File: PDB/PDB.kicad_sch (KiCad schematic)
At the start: 42 parts, among them Q1 S8050, Sw1 D-SWITCH_MR5-111-C5N-BB

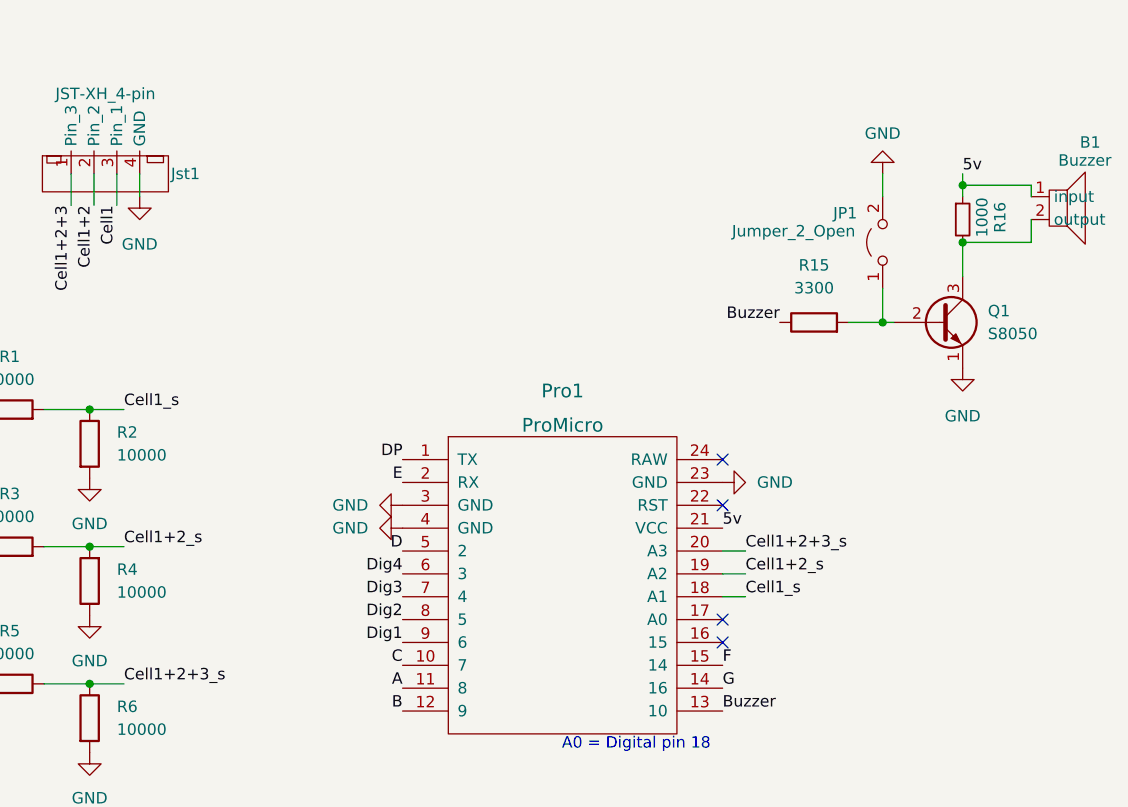
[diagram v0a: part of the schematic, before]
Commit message: Completed board layout
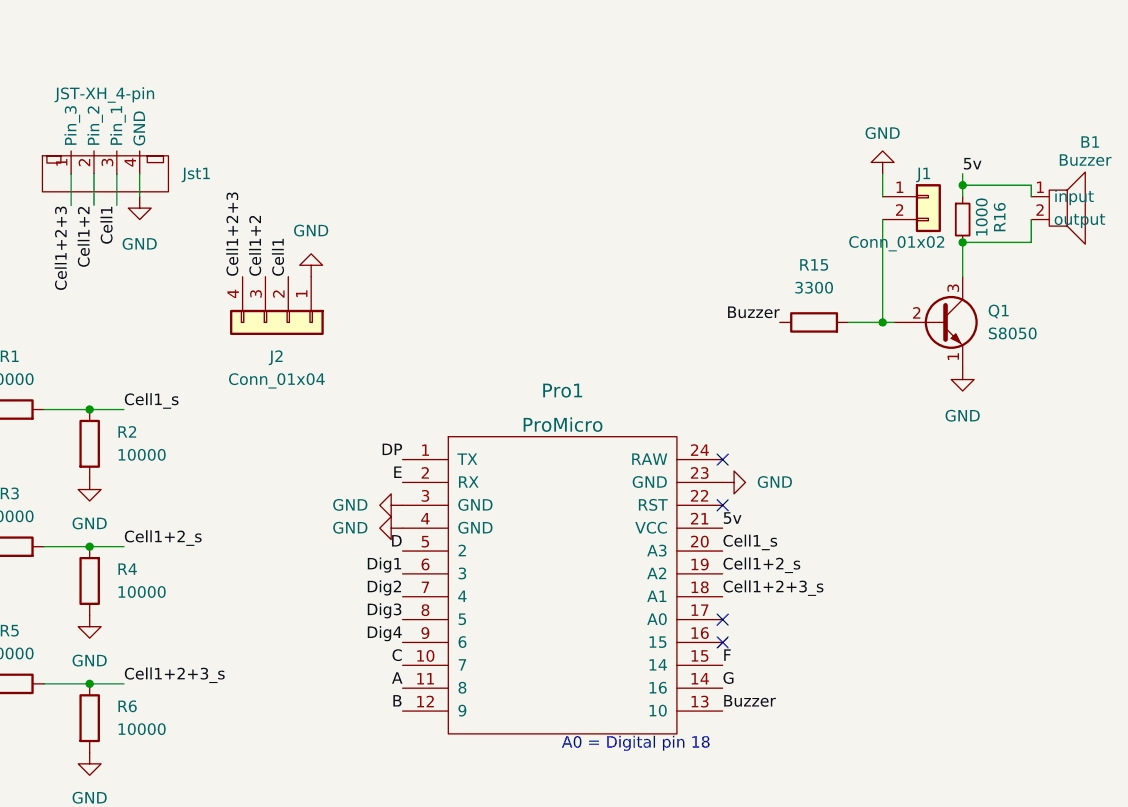
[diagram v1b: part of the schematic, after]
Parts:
- removed JP1: Jumper_2_Open, Connector_PinHeader_2.54mm:PinHeader_1x02_P2.54mm_Vertical, symbol Jumper:Jumper_2_Open
- added J1: Conn_01x02, Connector_PinHeader_2.54mm:PinHeader_1x02_P2.54mm_Vertical, symbol Connector_Generic:Conn_01x02
- added J2: Conn_01x04, Connector_PinHeader_2.54mm:PinHeader_1x04_P2.54mm_Vertical, symbol Connector_Generic:Conn_01x04
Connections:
- net Cell1: now also J2.2 (Pin_2)
- net Cell1+2: now also J2.3 (Pin_3)
- net Cell1+2+3: now also J2.4 (Pin_4)
- net Cell1+2+3_s: now also Pro1.18 (A1); no longer Pro1.20 (A3)
- net Cell1_s: now also Pro1.20 (A3); no longer Pro1.18 (A1)
- net Dig1: now also Pro1.6 (3); no longer Pro1.9 (6)
- net Dig2: now also Pro1.7 (4); no longer Pro1.8 (5)
- net Dig3: now also Pro1.8 (5); no longer Pro1.7 (4)
- net Dig4: now also Pro1.9 (6); no longer Pro1.6 (3)
- net GND: now also J1.1 (Pin_1), J2.1 (Pin_1)
- net at Q1.2 (B), R15.2: now also J1.2 (Pin_2)
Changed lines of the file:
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@@
-    (stroke (width 0) (type default) (color 0 0 0 0))
-  )
-  (wire (pts (xy 109.22 177.8) (xy 111.76 177.8))
     (stroke (width 0) (type default) (color 0 0 0 0))
   )
@@
     (stroke (width 0) (type default) (color 0 0 0 0))
   )
-  (wire (pts (xy 109.22 172.72) (xy 111.76 172.72))
-    (stroke (width 0) (type default) (color 0 0 0 0))
-  )
   (wire (pts (xy 36.83 130.81) (xy 36.83 134.31))
     (stroke (width 0) (type default) (color 0 0 0 0))
   )
-  (wire (pts (xy 127 143.51) (xy 127 147.32))
-    (stroke (width 0) (type default) (color 0 0 0 0))
-  )
-  (wire (pts (xy 109.22 175.26) (xy 111.76 175.26))
+  (wire (pts (xy 127 135.89) (xy 127 147.32))
     (stroke (width 0) (type default) (color 0 0 0 0))
   )
@@
     (effects (font (size 1.27 1.27)) (justify left bottom))
   )
-  (label "Cell1+2+3_s" (at 111.76 172.72 0)
+  (label "Cell1+2+3_s" (at 109.22 177.8 0)
     (effects (font (size 1.27 1.27)) (justify left bottom))
   )
@@
     (effects (font (size 1.27 1.27)) (justify right bottom))
   )
-  (label "Dig2" (at 73.66 180.34 180)
-    (effects (font (size 1.27 1.27)) (justify right bottom))
-  )
-  (label "Dig4" (at 73.66 175.26 180)
-    (effects (font (size 1.27 1.27)) (justify right bottom))
+  (label "Dig2" (at 73.66 177.8 180)
+    (effects (font (size 1.27 1.27)) (justify right bottom))
+  )
+  (label "Dig4" (at 73.66 182.88 180)
+    (effects (font (size 1.27 1.27)) (justify right bottom))
+  )
+  (label "Cell1+2+3" (at 55.88 142.24 90)
+    (effects (font (size 1.27 1.27)) (justify left bottom))
   )
   (label "12v" (at 53.41 55.45 0)
@@
     (effects (font (size 1.27 1.27)) (justify left bottom))
   )
+  (label "Cell1" (at 60.96 142.24 90)
+    (effects (font (size 1.27 1.27)) (justify left bottom))
+  )
   (label "Cell1+2+3" (at 36.83 134.31 270)
     (effects (font (size 1.27 1.27)) (justify right bottom))
@@
     (effects (font (size 1.27 1.27)) (justify left bottom))
   )
-  (label "Cell1_s" (at 111.76 177.8 0)
+  (label "Cell1_s" (at 109.22 172.72 0)
+    (effects (font (size 1.27 1.27)) (justify left bottom))
+  )
+  (label "Cell1+2" (at 58.42 142.24 90)
     (effects (font (size 1.27 1.27)) (justify left bottom))
   )
@@
     (effects (font (size 1.27 1.27)) (justify right bottom))
   )
-  (label "Dig3" (at 73.66 177.8 180)
+  (label "Dig3" (at 73.66 180.34 180)
     (effects (font (size 1.27 1.27)) (justify right bottom))
   )
@@
     (effects (font (size 1.27 1.27)) (justify right bottom))
   )
-  (label "Dig1" (at 73.66 182.88 180)
+  (label "Dig1" (at 73.66 175.26 180)
     (effects (font (size 1.27 1.27)) (justify right bottom))
   )
@@
     (effects (font (size 1.27 1.27)) (justify left bottom))
   )
-  (label "Cell1+2_s" (at 111.76 175.26 0)
+  (label "Cell1+2_s" (at 109.22 175.26 0)
     (effects (font (size 1.27 1.27)) (justify left bottom))
   )
@@
     )
     (pin "1")
-  )
-  (symbol (lib_id "Jumper:Jumper_2_Open") (at 127 138.43 90) (unit 1)
-    (in_bom yes) (on_board yes)
-    (property "Reference" "JP1" (id 0) (at 121.5 135.18 90)
-      (effects (font (size 1.27 1.27)) (justify right))
-    )
-    (property "Value" "Jumper_2_Open" (id 1) (at 110.25 137.18 90)
-      (effects (font (size 1.27 1.27)) (justify right))
-    )
-    (property "Footprint" "Connector_PinHeader_2.54mm:PinHeader_1x02_P2.54mm_Vertical" (id 2) (at 127 138.43 0)
-      (effects (font (size 1.27 1.27)) hide)
-    )
-    (property "Datasheet" "~" (id 3) (at 127 138.43 0)
-      (effects (font (size 1.27 1.27)) hide)
-    )
-    (pin "1")
-    (pin "2")
   )
   (symbol (lib_id "Device:R") (at 38.89 176.05 180) (unit 1)
@@
     (pin "1")
     (pin "2")
+  )
+  (symbol (lib_id "Connector_Generic:Conn_01x04") (at 60.96 147.32 270) (unit 1)
+    (in_bom yes) (on_board yes) (fields_autoplaced)
+    (property "Reference" "J2" (id 0) (at 59.69 151.13 90))
+    (property "Value" "Conn_01x04" (id 1) (at 59.69 153.67 90))
+    (property "Footprint" "Connector_PinHeader_2.54mm:PinHeader_1x04_P2.54mm_Vertical" (id 2) (at 60.96 147.32 0)
+      (effects (font (size 1.27 1.27)) hide)
+    )
+    (property "Datasheet" "~" (id 3) (at 60.96 147.32 0)
+      (effects (font (size 1.27 1.27)) hide)
+    )
+    (pin "1")
+    (pin "2")
+    (pin "3")
+    (pin "4")
   )
   (symbol (lib_id "Device:LED") (at 59.75 20.69 90) (unit 1)
@@
     (pin "2")
   )
+  (symbol (lib_id "Connector_Generic:Conn_01x02") (at 132.08 133.35 0) (unit 1)
+    (in_bom yes) (on_board yes)
+    (property "Reference" "J1" (id 0) (at 130.81 130.81 0)
+      (effects (font (size 1.27 1.27)) (justify left))
+    )
+    (property "Value" "Conn_01x02" (id 1) (at 123.19 138.43 0)
+      (effects (font (size 1.27 1.27)) (justify left))
+    )
+    (property "Footprint" "Connector_PinHeader_2.54mm:PinHeader_1x02_P2.54mm_Vertical" (id 2) (at 132.08 133.35 0)
+      (effects (font (size 1.27 1.27)) hide)
+    )
+    (property "Datasheet" "~" (id 3) (at 132.08 133.35 0)
+      (effects (font (size 1.27 1.27)) hide)
+    )
+    (pin "1")
+    (pin "2")
+  )
   (symbol (lib_id "power:GND") (at 202.25 54 0) (unit 1)
     (in_bom yes) (on_board yes) (fields_autoplaced)
@@
     (pin "2")
   )
+  (symbol (lib_id "power:GND") (at 63.5 142.24 180) (unit 1)
+    (in_bom yes) (on_board yes) (fields_autoplaced)
+    (property "Reference" "#PWR0135" (id 0) (at 63.5 135.89 0)
+      (effects (font (size 1.27 1.27)) hide)
+    )
+    (property "Value" "GND" (id 1) (at 63.5 137.16 0))
+    (property "Footprint" "" (id 2) (at 63.5 142.24 0)
+      (effects (font (size 1.27 1.27)) hide)
+    )
+    (property "Datasheet" "" (id 3) (at 63.5 142.24 0)
+      (effects (font (size 1.27 1.27)) hide)
+    )
+    (pin "1")
+  )
   (symbol (lib_id "power:GND") (at 29 22 0) (unit 1)
     (in_bom yes) (on_board yes) (fields_autoplaced)
@@
   (symbol (lib_id "PiE_Symbols:JST-XH_4-pin") (at 40.64 130.81 0) (unit 1)
     (in_bom yes) (on_board yes)
-    (property "Reference" "Jst1" (id 0) (at 49.53 130.81 0))
+    (property "Reference" "Jst1" (id 0) (at 50.8 130.81 0))
     (property "Value" "JST-XH_4-pin" (id 1) (at 40.64 121.92 0))
     (property "Footprint" "PiE_Footprints:JST_XH_B4B-XH-AM_1x04_P2.50mm_Vertical" (id 2) (at 40.64 130.81 0)
@@
       (reference "#PWR0134") (unit 1) (value "GND") (footprint "")
     )
+    (path "/caaed65e-7179-41e8-b483-f562d970d26a"
+      (reference "#PWR0135") (unit 1) (value "GND") (footprint "")
+    )
     (path "/cc06864b-7a29-42b8-ae65-4c9e7f6eecfb"
       (reference "A1") (unit 1) (value "Anderson_Horizontal") (footprint "PiE_Footprints:anderson_horizontal")
@@
       (reference "F1") (unit 1) (value "Fuseholder") (footprint "PiE_Footprints:Fuse Holder SMD")
     )
-    (path "/10f30e8c-8f7f-4227-85f3-577503ceca5a"
-      (reference "JP1") (unit 1) (value "Jumper_2_Open") (footprint "Connector_PinHeader_2.54mm:PinHeader_1x02_P2.54mm_Vertical")
+    (path "/b5391e58-ae85-443b-b507-bfa34b750291"
+      (reference "J1") (unit 1) (value "Conn_01x02") (footprint "Connector_PinHeader_2.54mm:PinHeader_1x02_P2.54mm_Vertical")
+    )
+    (path "/8d7c7279-3465-4639-90dd-d836f538bc0a"
+      (reference "J2") (unit 1) (value "Conn_01x04") (footprint "Connector_PinHeader_2.54mm:PinHeader_1x04_P2.54mm_Vertical")
     )
     (path "/ce442d8d-66e0-49f8-af5b-062e6c86581b"

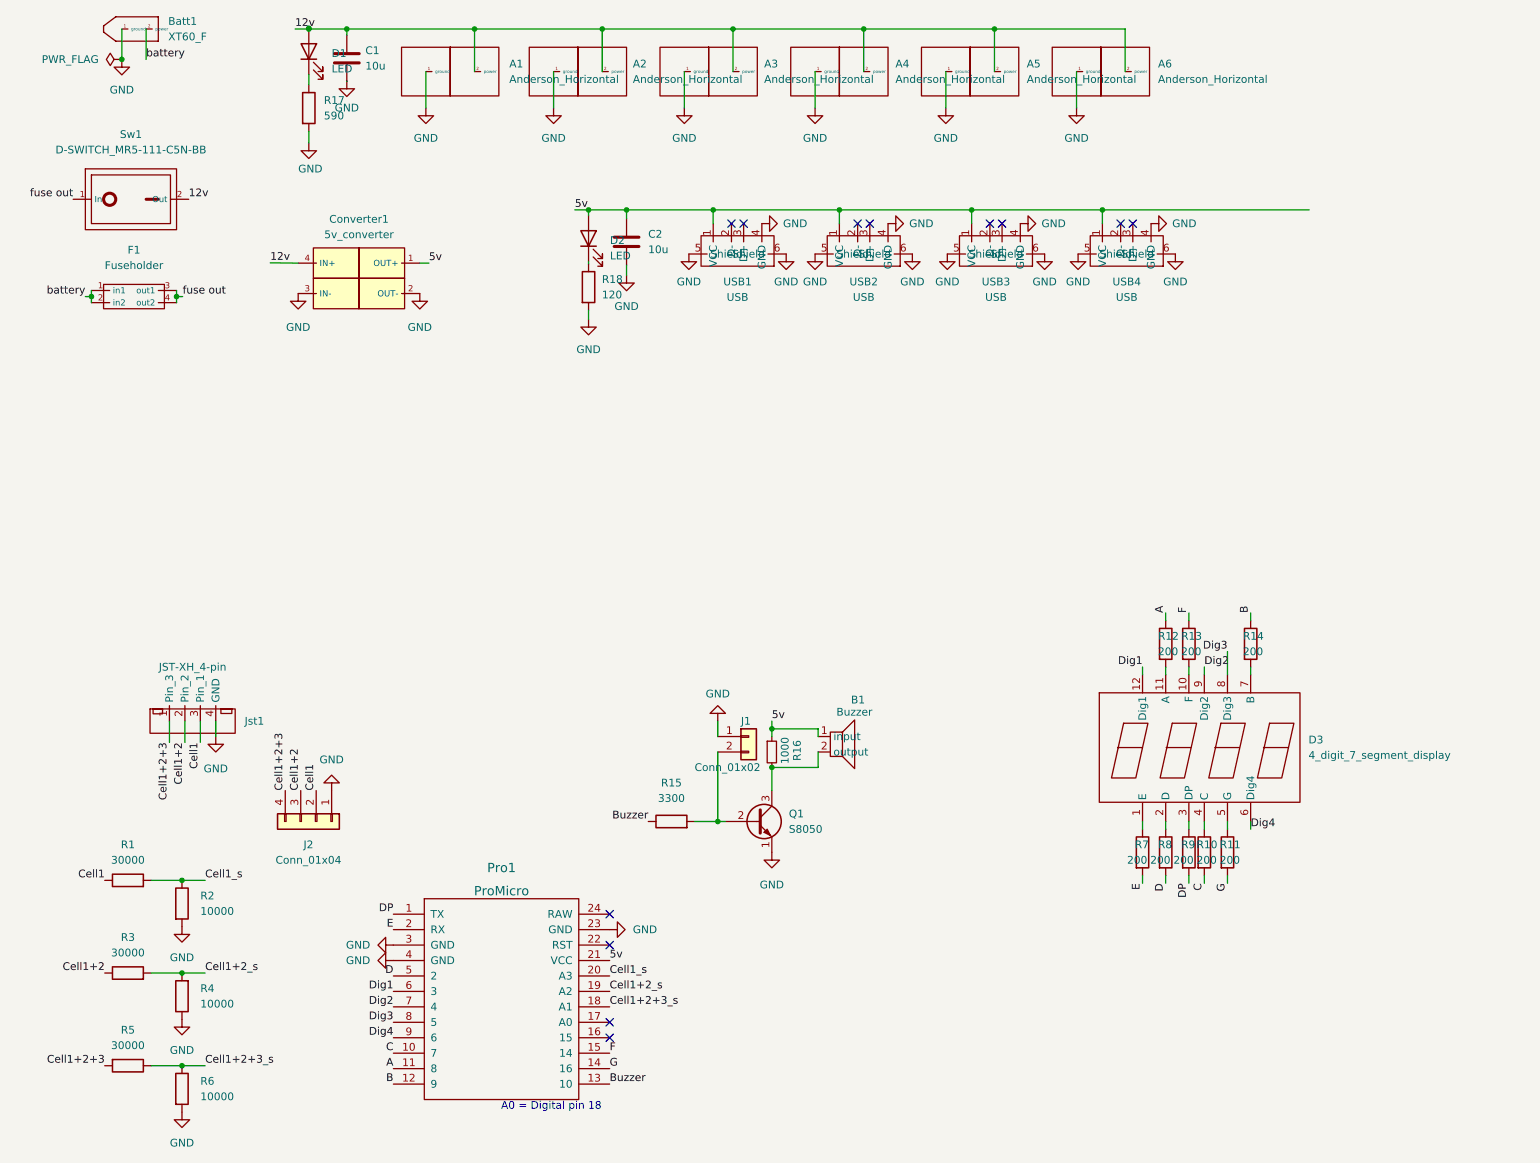
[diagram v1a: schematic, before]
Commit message: added FTDI chip
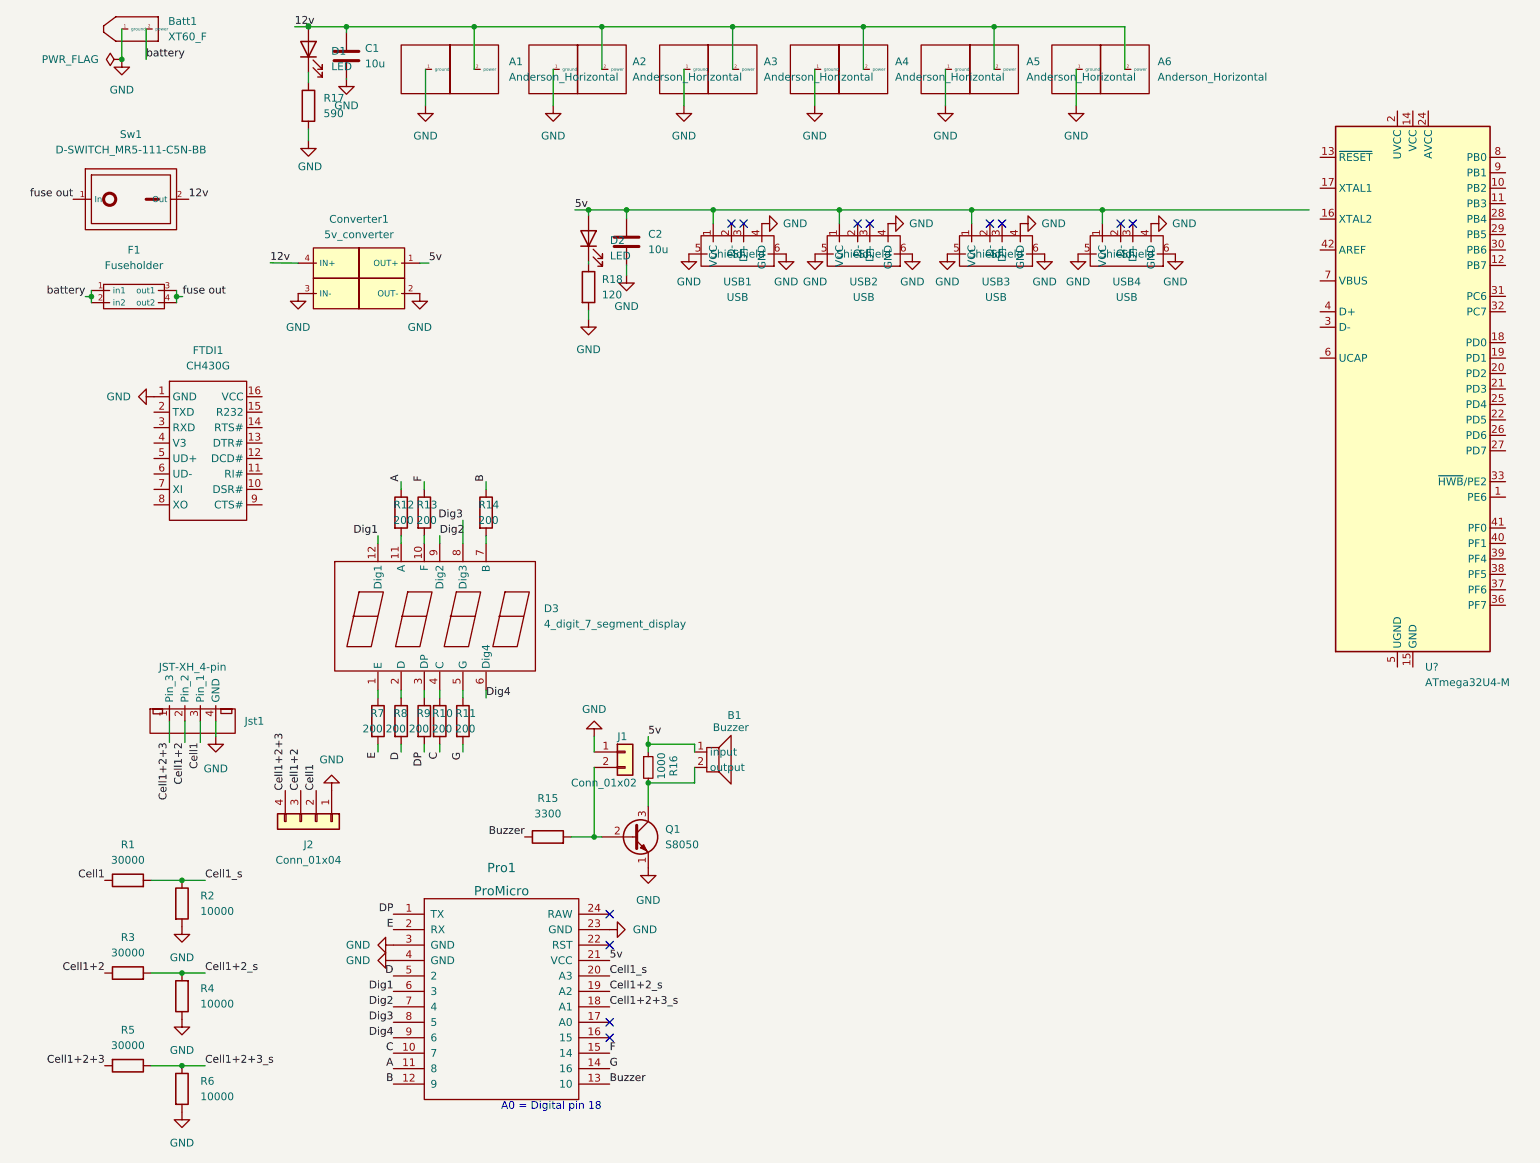
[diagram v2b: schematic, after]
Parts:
- added FTDI1: CH430G, symbol PiE_Symbols:CH430G
- added U?: ATmega32U4-M, Package_DFN_QFN:QFN-44-1EP_7x7mm_P0.5mm_EP5.2x5.2mm, symbol MCU_Microchip_ATmega:ATmega32U4-M
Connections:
- net GND: now also FTDI1.1 (GND)
- new net: U?.14 (VCC), U?.34 (VCC)
- new net: U?.15 (GND), U?.23 (GND), U?.35 (GND), U?.43 (GND), U?.45 (GND)
- new net: U?.24 (AVCC), U?.44 (AVCC)
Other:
- moved on the sheet: B1, D3, J1, Q1, R10, R11, R12, R13, R14, R15, R16, R7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
